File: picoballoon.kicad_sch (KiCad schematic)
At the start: 52 parts, among them J1 SOLAR+, J2 SOLAR-, Q1 AO3401A, Q2 DTC143ZEBTL, Q3 AO3401A, Q4 AO3401A, U1 SPV1040, U2 STM32G070RBTx, U3 L70-R, U4 GPS1003, U6 Ai-Thinker-Ra-01

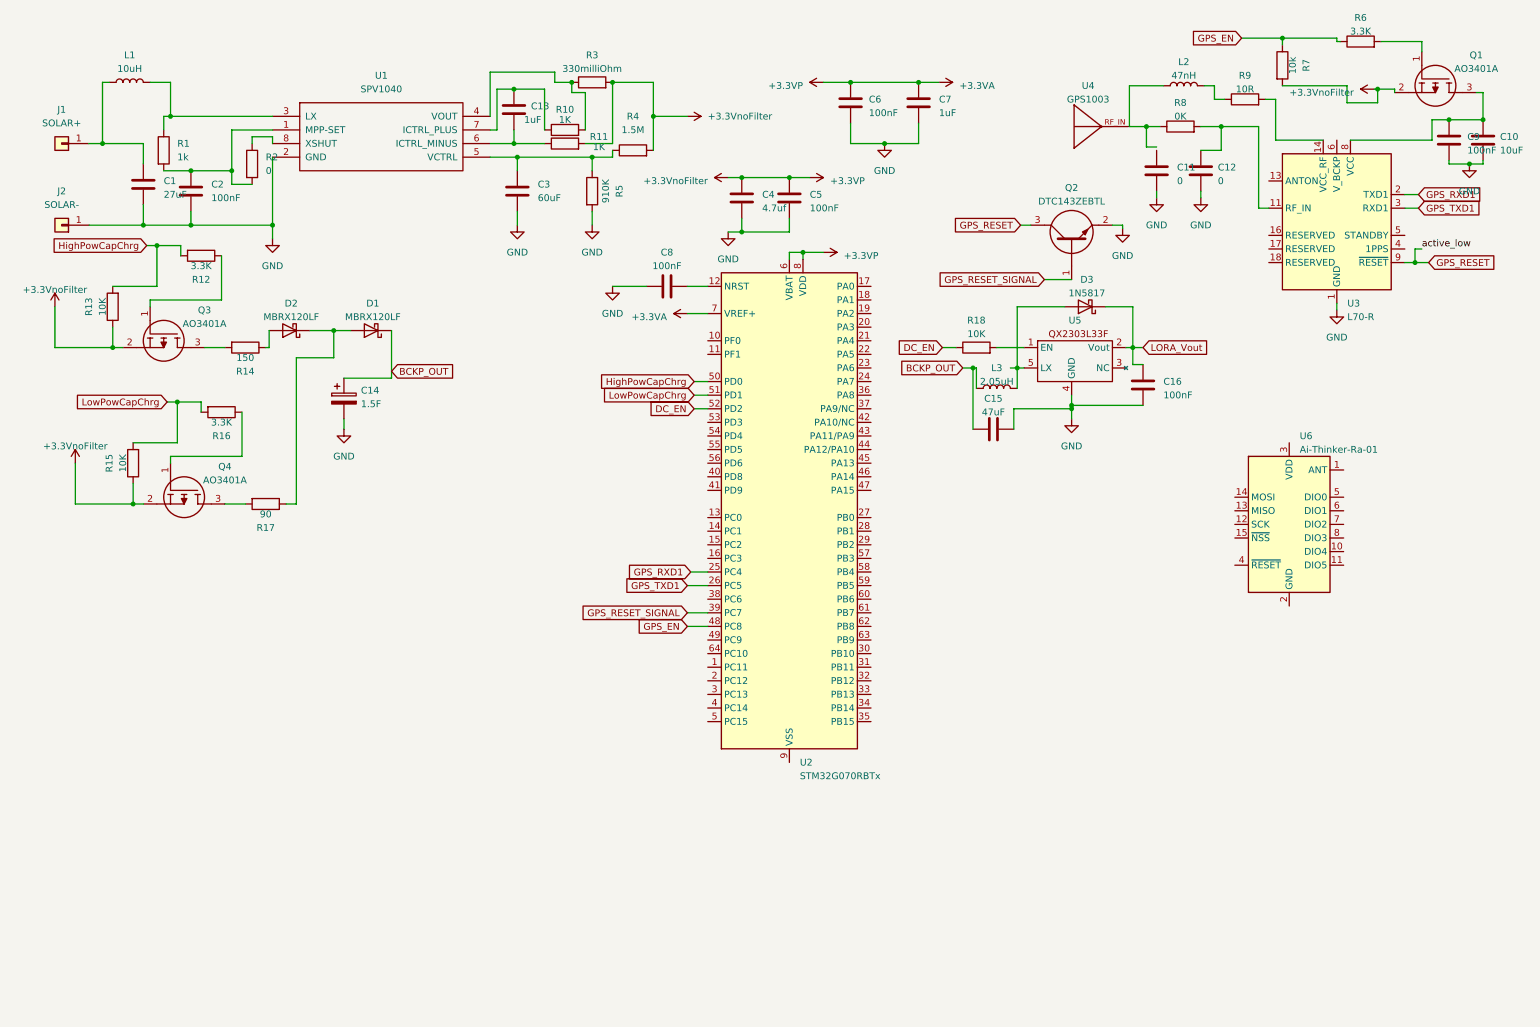
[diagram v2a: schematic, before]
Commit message: Finalized schematic and added all critical compoments. Minor tweaks will be added along the way.
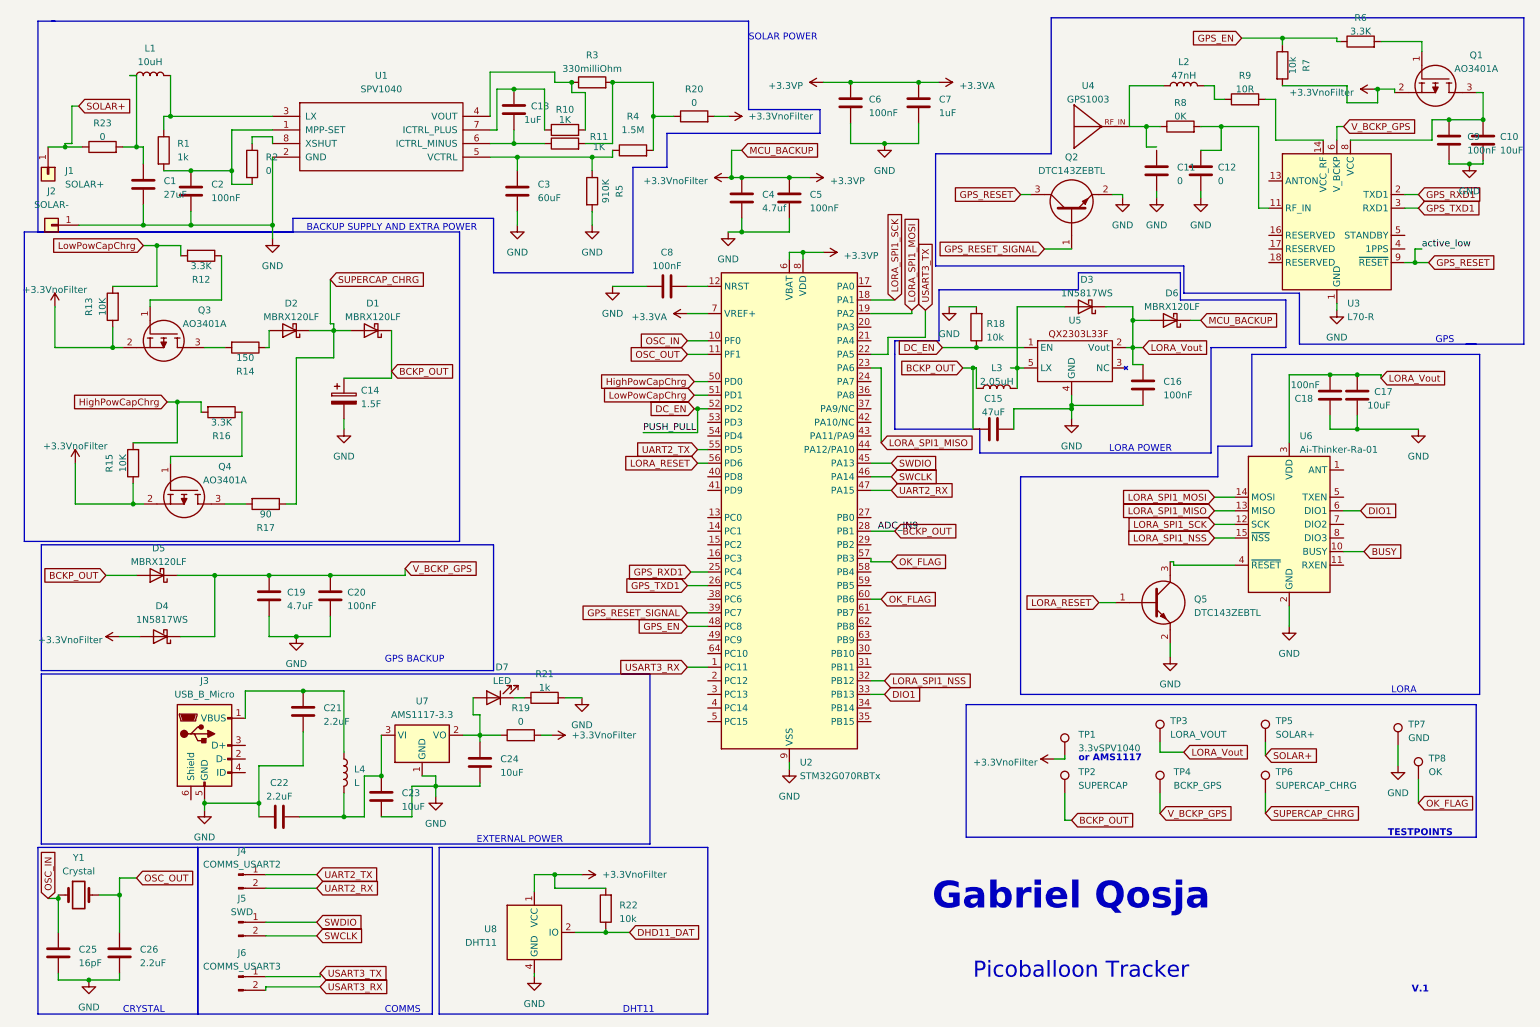
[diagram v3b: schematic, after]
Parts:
- added C17, C23, C24: 10uF, Capacitor_SMD:C_0201_0603Metric_Pad0.64x0.40mm_HandSolder, symbol Device:C
- added C18, C20: 100nF, Capacitor_SMD:C_0201_0603Metric_Pad0.64x0.40mm_HandSolder, symbol Device:C
- added C19: 4.7uF, Capacitor_SMD:C_0201_0603Metric_Pad0.64x0.40mm_HandSolder, symbol Device:C
- added C21, C22, C26: 2.2uF, Capacitor_SMD:C_0201_0603Metric_Pad0.64x0.40mm_HandSolder, symbol Device:C
- added C25: 16pF, Capacitor_SMD:C_0201_0603Metric_Pad0.64x0.40mm_HandSolder, symbol Device:C
- added D4: 1N5817WS, Diode_SMD:D_SOD-323, symbol Device:D_Schottky
- added D5, D6: MBRX120LF, Diode_SMD:D_SOD-123, symbol Device:D_Schottky
- added D7: LED, LED_THT:LED_D5.0mm, symbol Device:LED
- added J3: USB_B_Micro, Connector_USB:USB_Micro-B_Wuerth_629105150521, symbol Connector:USB_B_Micro
- added J4: COMMS_USART2, Connector_PinHeader_1.27mm:PinHeader_1x02_P1.27mm_Vertical, symbol Connector:Conn_01x02_Pin
- added J5: SWD, Connector_PinHeader_1.27mm:PinHeader_1x02_P1.27mm_Vertical, symbol Connector:Conn_01x02_Pin
- added J6: COMMS_USART3, Connector_PinHeader_1.27mm:PinHeader_1x02_P1.27mm_Vertical, symbol Connector:Conn_01x02_Pin
- added L4: L, Inductor_SMD:L_1206_3216Metric_Pad1.42x1.75mm_HandSolder, symbol Device:L
- added Q5: DTC143ZEBTL, Package_TO_SOT_SMD:SOT-523, symbol DTC143ZEBTL:DTC143ZEBTL
- added R19: 0, Resistor_SMD:R_0201_0603Metric, symbol Device:R
- added R20, R23: 0, Resistor_SMD:R_0201_0603Metric_Pad0.64x0.40mm_HandSolder, symbol Device:R
- added R21: 1k, Resistor_SMD:R_0201_0603Metric, symbol Device:R
- added R22: 10k, Resistor_SMD:R_0201_0603Metric, symbol Device:R
- added TP1: 3.3vSPV1040, TestPoint:TestPoint_Loop_D2.50mm_Drill1.0mm, symbol Connector:TestPoint
- added TP2: SUPERCAP, TestPoint:TestPoint_Loop_D2.50mm_Drill1.0mm, symbol Connector:TestPoint
- added TP3: LORA_VOUT, TestPoint:TestPoint_Loop_D2.50mm_Drill1.0mm, symbol Connector:TestPoint
- added TP4: BCKP_GPS, TestPoint:TestPoint_Loop_D2.50mm_Drill1.0mm, symbol Connector:TestPoint
- added TP5: SOLAR+, TestPoint:TestPoint_Loop_D2.50mm_Drill1.0mm, symbol Connector:TestPoint
- added TP6: SUPERCAP_CHRG, TestPoint:TestPoint_Loop_D2.50mm_Drill1.0mm, symbol Connector:TestPoint
- added TP7: GND, TestPoint:TestPoint_Loop_D2.50mm_Drill1.0mm, symbol Connector:TestPoint
- added TP8: OK, TestPoint:TestPoint_Loop_D3.80mm_Drill2.5mm, symbol Connector_custom:TestPoint
- added U7: AMS1117-3.3, Package_TO_SOT_SMD:SOT-223-3_TabPin2, symbol Regulator_Linear:AMS1117-3.3
- added U8: DHT11, Sensor:Aosong_DHT11_5.5x12.0_P2.54mm, symbol Sensor:DHT11
- added Y1: Crystal, Crystal:Crystal_HC49-U_Vertical, symbol Device:Crystal
- C1, C2, C3: footprint Capacitor_SMD:C_0201_0603Metric -> Capacitor_SMD:C_0201_0603Metric_Pad0.64x0.40mm_HandSolder
- C10, C11, C12, C13, C14, C15, C16, C4, C5, C6, C7, C8, C9: footprint (none) -> Capacitor_SMD:C_0201_0603Metric_Pad0.64x0.40mm_HandSolder
- D1, D2: footprint (none) -> Diode_SMD:D_SOD-123
- D3: value 1N5817 -> 1N5817WS; footprint Diode_THT:D_DO-41_SOD81_P10.16mm_Horizontal -> Diode_SMD:D_SOD-323
- J1, J2: footprint (none) -> Connector_Wire:SolderWire-1.5sqmm_1x01_D1.7mm_OD3.9mm
- L2: footprint (none) -> Inductor_SMD:L_0603_1608Metric_Pad1.05x0.95mm_HandSolder
- L3: footprint (none) -> Inductor_SMD:L_0201_0603Metric_Pad0.64x0.40mm_HandSolder
- Q1, Q3, Q4: footprint SOT95P280X125-3N -> Package_TO_SOT_SMD:SOT-23
- Q2: footprint SOTFL50P160X85-3N -> Package_TO_SOT_SMD:SOT-523
- R1, R2: footprint Resistor_SMD:R_0201_0603Metric -> Resistor_SMD:R_0201_0603Metric_Pad0.64x0.40mm_HandSolder
- R11, R12, R13, R14, R15, R16, R17, R3, R4, R5, R6, R7, R8, R9: footprint (none) -> Resistor_SMD:R_0201_0603Metric_Pad0.64x0.40mm_HandSolder
- R18: value 10K -> 10k; footprint (none) -> Resistor_SMD:R_0201_0603Metric
- U1: footprint (none) -> Package_SO:TSSOP-8_4.4x3mm_P0.65mm
- U5: footprint QX2303L33F:QX2303L33F -> Package_TO_SOT_SMD:SOT-23-5_HandSoldering
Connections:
- net +3.3V: now also D4.2 (A), D6.1 (K), R19.2, R20.2, R22.2, TP1.1, U8.1 (VCC); no longer R11.2, R3.2, R4.2
- net BCKP_OUT: now also U2.28 (PB1), D5.2 (A), TP2.1
- net DC_EN: now also U5.1 (EN)
- net GND: now also R18.2, U2.9 (VSS), U6.16 (GND), U6.2 (GND), U6.9 (GND), C17.1, C18.2, C19.2, C20.2, C21.2, C22.1, C23.2, C24.2, C25.1, C26.1, J3.5 (GND), Q5.2, R21.2, TP7.1, U7.1 (GND), U8.4 (GND)
- net HighPowCapChrg: now also R15.2, R16.2; no longer R12.2, R13.2
- net LORA_Vout: now also U6.3 (VDD), C17.2, C18.1, D6.2 (A), TP3.1
- net LowPowCapChrg: now also R12.2, R13.2; no longer R15.2, R16.2
- net at C1.1, L1.1: now also R23.2; no longer J1.1 (Pin_1)
- net USART3_RX: now reaches U2.1 (PC11)
- net USART3_RX: now also J6.2 (Pin_2)
- net OSC_IN: now reaches U2.10 (PF0)
- net OSC_IN: now also C25.2, Y1.1
- net OSC_OUT: now reaches U2.11 (PF1)
- net OSC_OUT: now also C26.2, Y1.2
- net LORA_SPI1_SCK: now reaches U2.18 (PA1)
- net LORA_SPI1_SCK: now also U6.12 (SCK)
- net LORA_SPI1_MOSI: now reaches U2.19 (PA2)
- net LORA_SPI1_MOSI: now also U6.14 (MOSI)
- net USART3_TX: now reaches U2.22 (PA5)
- net USART3_TX: now also J6.1 (Pin_1)
- net LORA_SPI1_MISO: now reaches U2.23 (PA6)
- net LORA_SPI1_MISO: now also U6.13 (MISO)
- net LORA_SPI1_NSS: now reaches U2.32 (PB12)
- net LORA_SPI1_NSS: now also U6.15 (~{NSS})
- net DIO1: now reaches U2.33 (PB13)
- net DIO1: now also U6.6 (DIO1)
- net SWDIO: now reaches U2.45 (PA13)
- net SWDIO: now also J5.1 (Pin_1)
- net SWCLK: now reaches U2.46 (PA14)
- net SWCLK: now also J5.2 (Pin_2)
- net UART2_RX: now reaches U2.47 (PA15)
- net UART2_RX: now also J4.2 (Pin_2)
- net UART2_TX: now reaches U2.55 (PD5)
- net UART2_TX: now also J4.1 (Pin_1)
- net LORA_RESET: now reaches U2.56 (PD6)
- net LORA_RESET: now also Q5.1
- net OK_FLAG: now reaches U2.57 (PB3)
- net OK_FLAG: now also U2.60 (PB6), TP8.1
- net V_BCKP_GPS: now reaches U3.6 (V_BCKP)
- net V_BCKP_GPS: now also C19.1, C20.1, D4.1 (K), D5.1 (K), TP4.1
- net SUPERCAP_CHRG: now reaches D1.2 (A), D2.1 (K), R17.1
- net SUPERCAP_CHRG: now also TP6.1
- net BUSY: now reaches U6.10 (BUSY)
- net at U6.4 (~{RESET}): now also Q5.3
- new net: C24.1, D7.2 (A), R19.1, U7.2 (VO)
- new net: R11.2, R20.1, R3.2, R4.2
- new net: C21.1, J3.1 (VBUS), L4.1
- new net: C22.2, C23.1, L4.2, U7.3 (VI)
- new net: D7.1 (K), R21.1
- new net DHD11_DAT: R22.1, U8.2 (IO)
- new net SOLAR+: J1.1 (Pin_1), R23.1, TP5.1
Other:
- note added: "BACKUP SUPPLY AND EXTRA POWER"
- note added: "COMMS"
- note added: "CRYSTAL"
- note added: "DHT11"
- note added: "EXTERNAL POWER"
- note added: "GPS"
- note added: "GPS BACKUP"
- note added: "Gabriel Qosja"
- note added: "LORA"
- note added: "LORA POWER"
- note added: "Picoballoon Tracker"
- note added: "SOLAR POWER"
- note added: "TESTPOINTS"
- note added: "V.1"
- note added: "or AMS1117"
- moved on the sheet: J1, J2, L1, Q2

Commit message: Completed PCB routing
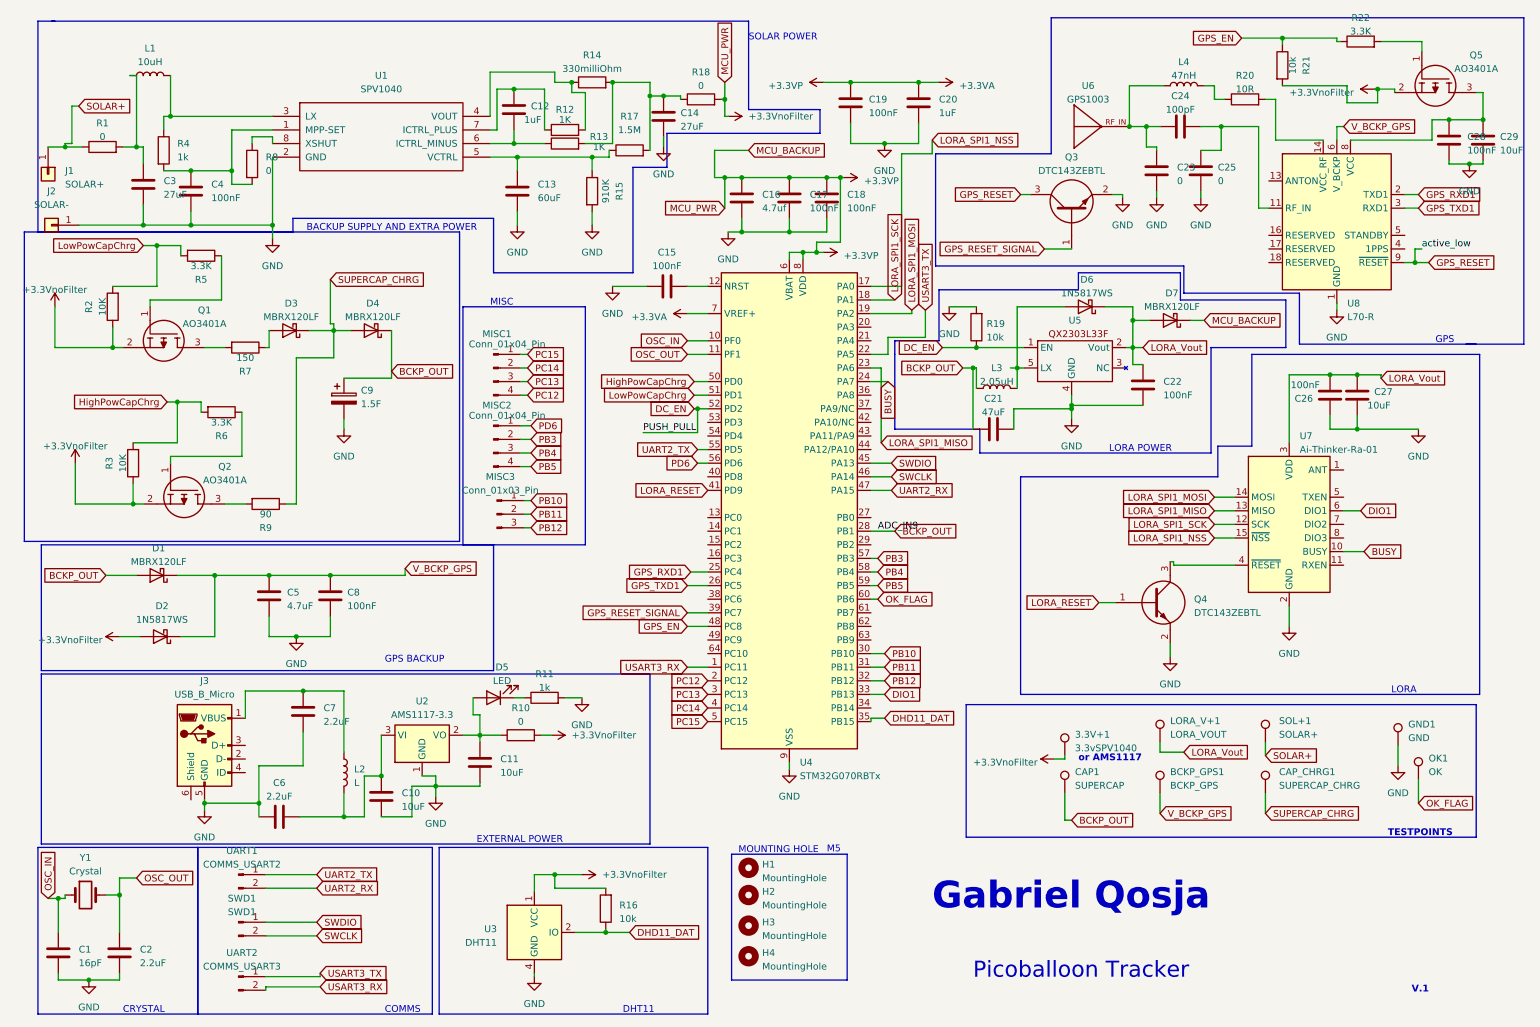
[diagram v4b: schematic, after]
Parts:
- removed R8: 0K, Resistor_SMD:R_0201_0603Metric_Pad0.64x0.40mm_HandSolder, symbol Device:R
- added C14: 27uF, Capacitor_SMD:C_0603_1608Metric, symbol Device:C
- added C18: 100nF, Capacitor_SMD:C_0603_1608Metric, symbol Device:C
- added C24: 100pF, Capacitor_SMD:C_0603_1608Metric, symbol Device:C
- added H1, H2, H3, H4: MountingHole, MountingHole:MountingHole_5.3mm_M5, symbol Mechanical:MountingHole
- added MISC1, MISC2: Conn_01x04_Pin, Connector_PinHeader_2.54mm:PinHeader_1x04_P2.54mm_Vertical, symbol Connector:Conn_01x04_Pin
- added MISC3: Conn_01x03_Pin, Connector_PinHeader_2.54mm:PinHeader_1x03_P2.54mm_Vertical, symbol Connector:Conn_01x03_Pin
- 3.3V+1: renamed from TP1; footprint TestPoint:TestPoint_Loop_D2.50mm_Drill1.0mm -> TestPoint:TestPoint_Pad_D3.0mm
- BCKP_GPS1: renamed from TP4; footprint TestPoint:TestPoint_Loop_D2.50mm_Drill1.0mm -> TestPoint:TestPoint_Pad_D3.0mm
- C1: renamed from C25; footprint Capacitor_SMD:C_0201_0603Metric_Pad0.64x0.40mm_HandSolder -> Capacitor_SMD:C_0603_1608Metric
- C10: renamed from C23; footprint Capacitor_SMD:C_0201_0603Metric_Pad0.64x0.40mm_HandSolder -> Capacitor_SMD:C_0603_1608Metric
- C11: renamed from C24; footprint Capacitor_SMD:C_0201_0603Metric_Pad0.64x0.40mm_HandSolder -> Capacitor_SMD:C_0603_1608Metric
- C12: renamed from C13; footprint Capacitor_SMD:C_0201_0603Metric_Pad0.64x0.40mm_HandSolder -> Capacitor_SMD:C_0603_1608Metric
- C13: renamed from C3; footprint Capacitor_SMD:C_0201_0603Metric_Pad0.64x0.40mm_HandSolder -> Capacitor_SMD:C_0603_1608Metric
- C15: renamed from C8; footprint Capacitor_SMD:C_0201_0603Metric_Pad0.64x0.40mm_HandSolder -> Capacitor_SMD:C_0603_1608Metric
- C16: renamed from C4; footprint Capacitor_SMD:C_0201_0603Metric_Pad0.64x0.40mm_HandSolder -> Capacitor_SMD:C_0603_1608Metric
- C17: renamed from C5; footprint Capacitor_SMD:C_0201_0603Metric_Pad0.64x0.40mm_HandSolder -> Capacitor_SMD:C_0603_1608Metric
- C19: renamed from C6; footprint Capacitor_SMD:C_0201_0603Metric_Pad0.64x0.40mm_HandSolder -> Capacitor_SMD:C_0603_1608Metric
- C2: renamed from C26; footprint Capacitor_SMD:C_0201_0603Metric_Pad0.64x0.40mm_HandSolder -> Capacitor_SMD:C_0603_1608Metric
- C20: renamed from C7; footprint Capacitor_SMD:C_0201_0603Metric_Pad0.64x0.40mm_HandSolder -> Capacitor_SMD:C_0603_1608Metric
- C21: renamed from C15; footprint Capacitor_SMD:C_0201_0603Metric_Pad0.64x0.40mm_HandSolder -> Capacitor_SMD:C_0603_1608Metric
- C22: renamed from C16; footprint Capacitor_SMD:C_0201_0603Metric_Pad0.64x0.40mm_HandSolder -> Capacitor_SMD:C_0603_1608Metric
- C23: renamed from C11; footprint Capacitor_SMD:C_0201_0603Metric_Pad0.64x0.40mm_HandSolder -> Capacitor_SMD:C_0603_1608Metric
- C25: renamed from C12; footprint Capacitor_SMD:C_0201_0603Metric_Pad0.64x0.40mm_HandSolder -> Capacitor_SMD:C_0603_1608Metric
- C26: renamed from C18; footprint Capacitor_SMD:C_0201_0603Metric_Pad0.64x0.40mm_HandSolder -> Capacitor_SMD:C_0603_1608Metric
- C27: renamed from C17; footprint Capacitor_SMD:C_0201_0603Metric_Pad0.64x0.40mm_HandSolder -> Capacitor_SMD:C_0603_1608Metric
- C28: renamed from C9; footprint Capacitor_SMD:C_0201_0603Metric_Pad0.64x0.40mm_HandSolder -> Capacitor_SMD:C_0603_1608Metric
- C29: renamed from C10; footprint Capacitor_SMD:C_0201_0603Metric_Pad0.64x0.40mm_HandSolder -> Capacitor_SMD:C_0603_1608Metric
- C3: renamed from C1; footprint Capacitor_SMD:C_0201_0603Metric_Pad0.64x0.40mm_HandSolder -> Capacitor_SMD:C_0603_1608Metric
- C4: renamed from C2; footprint Capacitor_SMD:C_0201_0603Metric_Pad0.64x0.40mm_HandSolder -> Capacitor_SMD:C_0603_1608Metric
- C5: renamed from C19; footprint Capacitor_SMD:C_0201_0603Metric_Pad0.64x0.40mm_HandSolder -> Capacitor_SMD:C_0603_1608Metric
- C6: renamed from C22; footprint Capacitor_SMD:C_0201_0603Metric_Pad0.64x0.40mm_HandSolder -> Capacitor_SMD:C_0603_1608Metric
- C7: renamed from C21; footprint Capacitor_SMD:C_0201_0603Metric_Pad0.64x0.40mm_HandSolder -> Capacitor_SMD:C_0603_1608Metric
- C8: renamed from C20; footprint Capacitor_SMD:C_0201_0603Metric_Pad0.64x0.40mm_HandSolder -> Capacitor_SMD:C_0603_1608Metric
- C9: renamed from C14; footprint Capacitor_SMD:C_0201_0603Metric_Pad0.64x0.40mm_HandSolder -> supercap:CP_Radial_D20mm_P5mm
- CAP1: renamed from TP2; footprint TestPoint:TestPoint_Loop_D2.50mm_Drill1.0mm -> TestPoint:TestPoint_Pad_D3.0mm
- CAP_CHRG1: renamed from TP6; footprint TestPoint:TestPoint_Loop_D2.50mm_Drill1.0mm -> TestPoint:TestPoint_Pad_D3.0mm
- GND1: renamed from TP7; footprint TestPoint:TestPoint_Loop_D2.50mm_Drill1.0mm -> TestPoint:TestPoint_Pad_D3.0mm
- L1: footprint Inductor_SMD:L_0201_0603Metric -> Inductor_SMD:L_0603_1608Metric
- L3: footprint Inductor_SMD:L_0201_0603Metric_Pad0.64x0.40mm_HandSolder -> Inductor_SMD:L_0603_1608Metric
- L4: renamed from L2; footprint Inductor_SMD:L_0603_1608Metric_Pad1.05x0.95mm_HandSolder -> Inductor_SMD:L_0603_1608Metric
- LORA_V+1: renamed from TP3; footprint TestPoint:TestPoint_Loop_D2.50mm_Drill1.0mm -> TestPoint:TestPoint_Pad_D3.0mm
- OK1: renamed from TP8; footprint TestPoint:TestPoint_Loop_D3.80mm_Drill2.5mm -> TestPoint:TestPoint_Pad_D3.0mm
- R1: renamed from R23; footprint Resistor_SMD:R_0201_0603Metric_Pad0.64x0.40mm_HandSolder -> Resistor_SMD:R_0603_1608Metric
- R10: renamed from R19; footprint Resistor_SMD:R_0201_0603Metric -> Resistor_SMD:R_0603_1608Metric
- R11: renamed from R21; footprint Resistor_SMD:R_0201_0603Metric -> Resistor_THT:R_Axial_DIN0204_L3.6mm_D1.6mm_P2.54mm_Vertical
- R12: renamed from R10; footprint Resistor_SMD:R_0201_0603Metric -> Resistor_SMD:R_0603_1608Metric
- R13: renamed from R11; footprint Resistor_SMD:R_0201_0603Metric_Pad0.64x0.40mm_HandSolder -> Resistor_SMD:R_0603_1608Metric
- R14: renamed from R3; footprint Resistor_SMD:R_0201_0603Metric_Pad0.64x0.40mm_HandSolder -> Resistor_SMD:R_0603_1608Metric
- R15: renamed from R5; footprint Resistor_SMD:R_0201_0603Metric_Pad0.64x0.40mm_HandSolder -> Resistor_SMD:R_0603_1608Metric
- R16: renamed from R22; footprint Resistor_SMD:R_0201_0603Metric -> Resistor_SMD:R_0603_1608Metric
- R17: renamed from R4; footprint Resistor_SMD:R_0201_0603Metric_Pad0.64x0.40mm_HandSolder -> Resistor_SMD:R_0603_1608Metric
- R18: renamed from R20; footprint Resistor_SMD:R_0201_0603Metric_Pad0.64x0.40mm_HandSolder -> Resistor_SMD:R_0603_1608Metric
- R19: renamed from R18; footprint Resistor_SMD:R_0201_0603Metric -> Resistor_THT:R_Axial_DIN0204_L3.6mm_D1.6mm_P2.54mm_Vertical
- R2: renamed from R13; footprint Resistor_SMD:R_0201_0603Metric_Pad0.64x0.40mm_HandSolder -> Resistor_THT:R_Axial_DIN0204_L3.6mm_D1.6mm_P2.54mm_Vertical
- R20: renamed from R9; footprint Resistor_SMD:R_0201_0603Metric_Pad0.64x0.40mm_HandSolder -> Resistor_SMD:R_0603_1608Metric
- R21: renamed from R7; footprint Resistor_SMD:R_0201_0603Metric_Pad0.64x0.40mm_HandSolder -> Resistor_THT:R_Axial_DIN0204_L3.6mm_D1.6mm_P2.54mm_Vertical
- R22: renamed from R6; footprint Resistor_SMD:R_0201_0603Metric_Pad0.64x0.40mm_HandSolder -> Resistor_SMD:R_0603_1608Metric
- R3: renamed from R15; footprint Resistor_SMD:R_0201_0603Metric_Pad0.64x0.40mm_HandSolder -> Resistor_THT:R_Axial_DIN0204_L3.6mm_D1.6mm_P2.54mm_Vertical
- R4: renamed from R1; footprint Resistor_SMD:R_0201_0603Metric_Pad0.64x0.40mm_HandSolder -> Resistor_SMD:R_0603_1608Metric
- R5: renamed from R12; footprint Resistor_SMD:R_0201_0603Metric_Pad0.64x0.40mm_HandSolder -> Resistor_SMD:R_0603_1608Metric
- R6: renamed from R16; footprint Resistor_SMD:R_0201_0603Metric_Pad0.64x0.40mm_HandSolder -> Resistor_SMD:R_0603_1608Metric
- R7: renamed from R14; footprint Resistor_SMD:R_0201_0603Metric_Pad0.64x0.40mm_HandSolder -> Resistor_SMD:R_0603_1608Metric
- R8: renamed from R2; footprint Resistor_SMD:R_0201_0603Metric_Pad0.64x0.40mm_HandSolder -> Resistor_SMD:R_0603_1608Metric
- R9: renamed from R17; footprint Resistor_SMD:R_0201_0603Metric_Pad0.64x0.40mm_HandSolder -> Resistor_SMD:R_0603_1608Metric
- SOL+1: renamed from TP5; footprint TestPoint:TestPoint_Loop_D2.50mm_Drill1.0mm -> TestPoint:TestPoint_Pad_D3.0mm
- SWD1: renamed from J5; value SWD -> SWD1
- renumbered D5 to D1, D4 to D2, D2 to D3, D1 to D4, D7 to D5, D3 to D6, D6 to D7, L4 to L2, Q3 to Q1, Q4 to Q2, Q2 to Q3, Q5 to Q4, Q1 to Q5, U7 to U2, U8 to U3, U2 to U4, U4 to U6, U6 to U7, U3 to U8, J4 to UART1, J6 to UART2
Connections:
- net +3.3V: now also C18.1
- net BUSY: now also U4.24 (PA7)
- net DHD11_DAT: now also U4.35 (PB15)
- net GND: now also C14.2, C18.2
- net LORA_RESET: now also U4.41 (PD9); no longer U4.56 (PD6)
- net LORA_SPI1_NSS: now also U4.17 (PA0); no longer U4.32 (PB12)
- net OK_FLAG: no longer U4.57 (PB3)
- net PC12: now reaches U4.2 (PC12)
- net PC12: now also MISC1.4 (Pin_4)
- net PC13: now reaches U4.3 (PC13)
- net PC13: now also MISC1.3 (Pin_3)
- net PB10: now reaches U4.30 (PB10)
- net PB10: now also MISC3.1 (Pin_1)
- net PB11: now reaches U4.31 (PB11)
- net PB11: now also MISC3.2 (Pin_2)
- net PC14: now reaches U4.4 (PC14)
- net PC14: now also MISC1.2 (Pin_2)
- net PC15: now reaches U4.5 (PC15)
- net PC15: now also MISC1.1 (Pin_1)
- net PB4: now reaches U4.58 (PB4)
- net PB4: now also MISC2.3 (Pin_3)
- net PB5: now reaches U4.59 (PB5)
- net PB5: now also MISC2.4 (Pin_4)
- net at C25.1, U8.11 (RF_IN): now also C24.2
- net at R13.2, R14.2, R17.2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: now also C14.1
- net at L4.1: now also C23.1, U6.RF_IN, C24.1
- new net PB12: MISC3.3 (Pin_3), U4.32 (PB12)
- new net PB3: MISC2.2 (Pin_2), U4.57 (PB3)
- new net PD6: MISC2.1 (Pin_1), U4.56 (PD6)
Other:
- note added: "M5"
- note added: "MISC"
- note added: "MOUNTING HOLE"
- moved on the sheet: R17, R18, Y1
